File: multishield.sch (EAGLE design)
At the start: 15 parts, among them J1 3p-2.54, J2 2x16p-2.54, J4 2x6p-2.54, K2 TS-1101F, M1 ARDUINO_R3_ICSP, Q1 BC547CZ1G, SW1 SK-12D01, U1 AD595AQ-DIP14, U2 ATMEGA328P_PDIP

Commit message: various improvements + clock
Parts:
- removed Q1: BC547CZ1G, Seeed-OPL-Transistor:DIP-TRANSISTOR-NPN-45V-0.1A-BC547CZ1G(TO-92)
- added C2, C3: 22pf, Seeed-OPL-Capacitor:DIP-CERAMIC-DISC-22PF-50V-10%-NPO(D4.0MM)
- added Q2: (no value), SparkFun-DiscreteSemi:TRANSISTOR_NPNBC547
- added Y1: 16MHZ, Seeed-OPL-Crystal-Oscillator:DIP-CRYSTAL-16MHZ-18PF-30PPM-50R(HC49US)
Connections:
- new net N$55: C2.2, U2.PB7(XTAL2/TOSC2), Y1.2
- new net N$57: C3.1, U2.PB6(XTAL1/TOSC1), Y1.1
- net GND: now also C2.1, C3.2, Q2.E; no longer Q1.E
- net N$36: now also Q2.C; no longer Q1.C
- net N$38: now also Q2.B; no longer Q1.B
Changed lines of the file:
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@@
 <part name="K2" library="Seeed-OPL-Button" deviceset="DIP-BUTTON-FRONT-WHITE(2P-3.4X6MM)" device="" value="TS-1101F"/>
 <part name="C1" library="Seeed-OPL-Capacitor" deviceset="DIP-CAP-ALUMINUM-47UF-16V(D5-H9MM)" device="" value="100µF/16V  5X7"/>
-<part name="Q1" library="Seeed-OPL-Transistor" deviceset="DIP-TRANSISTOR-NPN-45V-0.1A-BC547CZ1G(TO-92)" device="" value="BC547CZ1G"/>
 <part name="GND5" library="supply1" deviceset="GND" device=""/>
 <part name="R1" library="Seeed-OPL-Resistor" deviceset="DIP-RES-1K-5%-1/4W(PR-D2.3XL6.5MM)" device="" value="1K"/>
@@
 <part name="GND6" library="supply1" deviceset="GND" device=""/>
 <part name="P+7" library="supply1" deviceset="VCC" device=""/>
+<part name="Y1" library="Seeed-OPL-Crystal-Oscillator" deviceset="DIP-CRYSTAL-16MHZ-18PF-30PPM-50R(HC49US)" device="" value="16MHZ"/>
+<part name="C2" library="Seeed-OPL-Capacitor" deviceset="DIP-CERAMIC-DISC-22PF-50V-10%-NPO(D4.0MM)" device="" value="22pf"/>
+<part name="C3" library="Seeed-OPL-Capacitor" deviceset="DIP-CERAMIC-DISC-22PF-50V-10%-NPO(D4.0MM)" device="" value="22pf"/>
+<part name="GND9" library="supply1" deviceset="GND" device=""/>
+<part name="Q2" library="SparkFun-DiscreteSemi" deviceset="TRANSISTOR_NPN" device="BC547"/>
 </parts>
 <sheets>
@@
 <instance part="K2" gate="G$1" x="318.77" y="45.72"/>
 <instance part="C1" gate="G$1" x="187.96" y="172.72"/>
-<instance part="Q1" gate="G$1" x="194.31" y="177.8" rot="R180"/>
 <instance part="GND5" gate="1" x="191.77" y="185.42" rot="R180"/>
 <instance part="R1" gate="G$1" x="208.28" y="177.8"/>
@@
 <instance part="GND6" gate="1" x="87.63" y="66.04" rot="R270"/>
 <instance part="P+7" gate="VCC" x="87.63" y="69.85" rot="R90"/>
+<instance part="Y1" gate="G$1" x="316.23" y="82.55" rot="R90"/>
+<instance part="C2" gate="G$1" x="321.31" y="91.44" rot="R180"/>
+<instance part="C3" gate="G$1" x="321.31" y="74.93"/>
+<instance part="GND9" gate="1" x="327.66" y="83.82" rot="R90"/>
+<instance part="Q2" gate="G$1" x="194.31" y="177.8" rot="R180"/>
 </instances>
 <busses>
@@
 </segment>
 <segment>
-<pinref part="Q1" gate="G$1" pin="E"/>
-<pinref part="GND5" gate="1" pin="GND"/>
-</segment>
-<segment>
 <pinref part="J1" gate="G$1" pin="P$3"/>
 <pinref part="GND6" gate="1" pin="GND"/>
+</segment>
+<segment>
+<pinref part="C3" gate="G$1" pin="2"/>
+<pinref part="C2" gate="G$1" pin="1"/>
+<wire x1="325.12" y1="74.93" x2="325.12" y2="83.82" width="0.1524" layer="91"/>
+<junction x="325.12" y="83.82"/>
+<wire x1="325.12" y1="83.82" x2="325.12" y2="91.44" width="0.1524" layer="91"/>
+<pinref part="GND9" gate="1" pin="GND"/>
+</segment>
+<segment>
+<pinref part="GND5" gate="1" pin="GND"/>
+<pinref part="Q2" gate="G$1" pin="E"/>
 </segment>
 </net>
@@
 </segment>
 </net>
-<net name="N$36" class="0">
-<segment>
-<pinref part="C1" gate="G$1" pin="-"/>
-<pinref part="Q1" gate="G$1" pin="C"/>
-</segment>
-</net>
 <net name="N$37" class="0">
 <segment>
@@
 <net name="N$38" class="0">
 <segment>
-<pinref part="Q1" gate="G$1" pin="B"/>
 <wire x1="204.47" y1="177.8" x2="196.85" y2="177.8" width="0.1524" layer="91"/>
 <pinref part="R1" gate="G$1" pin="1"/>
+<pinref part="Q2" gate="G$1" pin="B"/>
 </segment>
 </net>
@@
 </segment>
 </net>
+<net name="N$55" class="0">
+<segment>
+<pinref part="U2" gate="G$1" pin="PB7(XTAL2/TOSC2)"/>
+<wire x1="304.8" y1="85.09" x2="307.34" y2="85.09" width="0.1524" layer="91"/>
+<wire x1="307.34" y1="85.09" x2="307.34" y2="88.9" width="0.1524" layer="91"/>
+<wire x1="307.34" y1="88.9" x2="316.23" y2="88.9" width="0.1524" layer="91"/>
+<pinref part="Y1" gate="G$1" pin="2"/>
+<wire x1="316.23" y1="88.9" x2="316.23" y2="86.36" width="0.1524" layer="91"/>
+<junction x="316.23" y="88.9"/>
+<wire x1="316.23" y1="88.9" x2="316.23" y2="91.44" width="0.1524" layer="91"/>
+<pinref part="C2" gate="G$1" pin="2"/>
+<wire x1="316.23" y1="91.44" x2="317.5" y2="91.44" width="0.1524" layer="91"/>
+</segment>
+</net>
+<net name="N$57" class="0">
+<segment>
+<pinref part="U2" gate="G$1" pin="PB6(XTAL1/TOSC1)"/>
+<wire x1="304.8" y1="80.01" x2="307.34" y2="80.01" width="0.1524" layer="91"/>
+<wire x1="307.34" y1="80.01" x2="307.34" y2="77.47" width="0.1524" layer="91"/>
+<wire x1="307.34" y1="77.47" x2="316.23" y2="77.47" width="0.1524" layer="91"/>
+<pinref part="Y1" gate="G$1" pin="1"/>
+<wire x1="316.23" y1="77.47" x2="316.23" y2="78.74" width="0.1524" layer="91"/>
+<junction x="316.23" y="77.47"/>
+<wire x1="316.23" y1="77.47" x2="316.23" y2="74.93" width="0.1524" layer="91"/>
+<pinref part="C3" gate="G$1" pin="1"/>
+<wire x1="316.23" y1="74.93" x2="317.5" y2="74.93" width="0.1524" layer="91"/>
+</segment>
+</net>
+<net name="N$36" class="0">
+<segment>
+<pinref part="C1" gate="G$1" pin="-"/>
+<pinref part="Q2" gate="G$1" pin="C"/>
+</segment>
+</net>

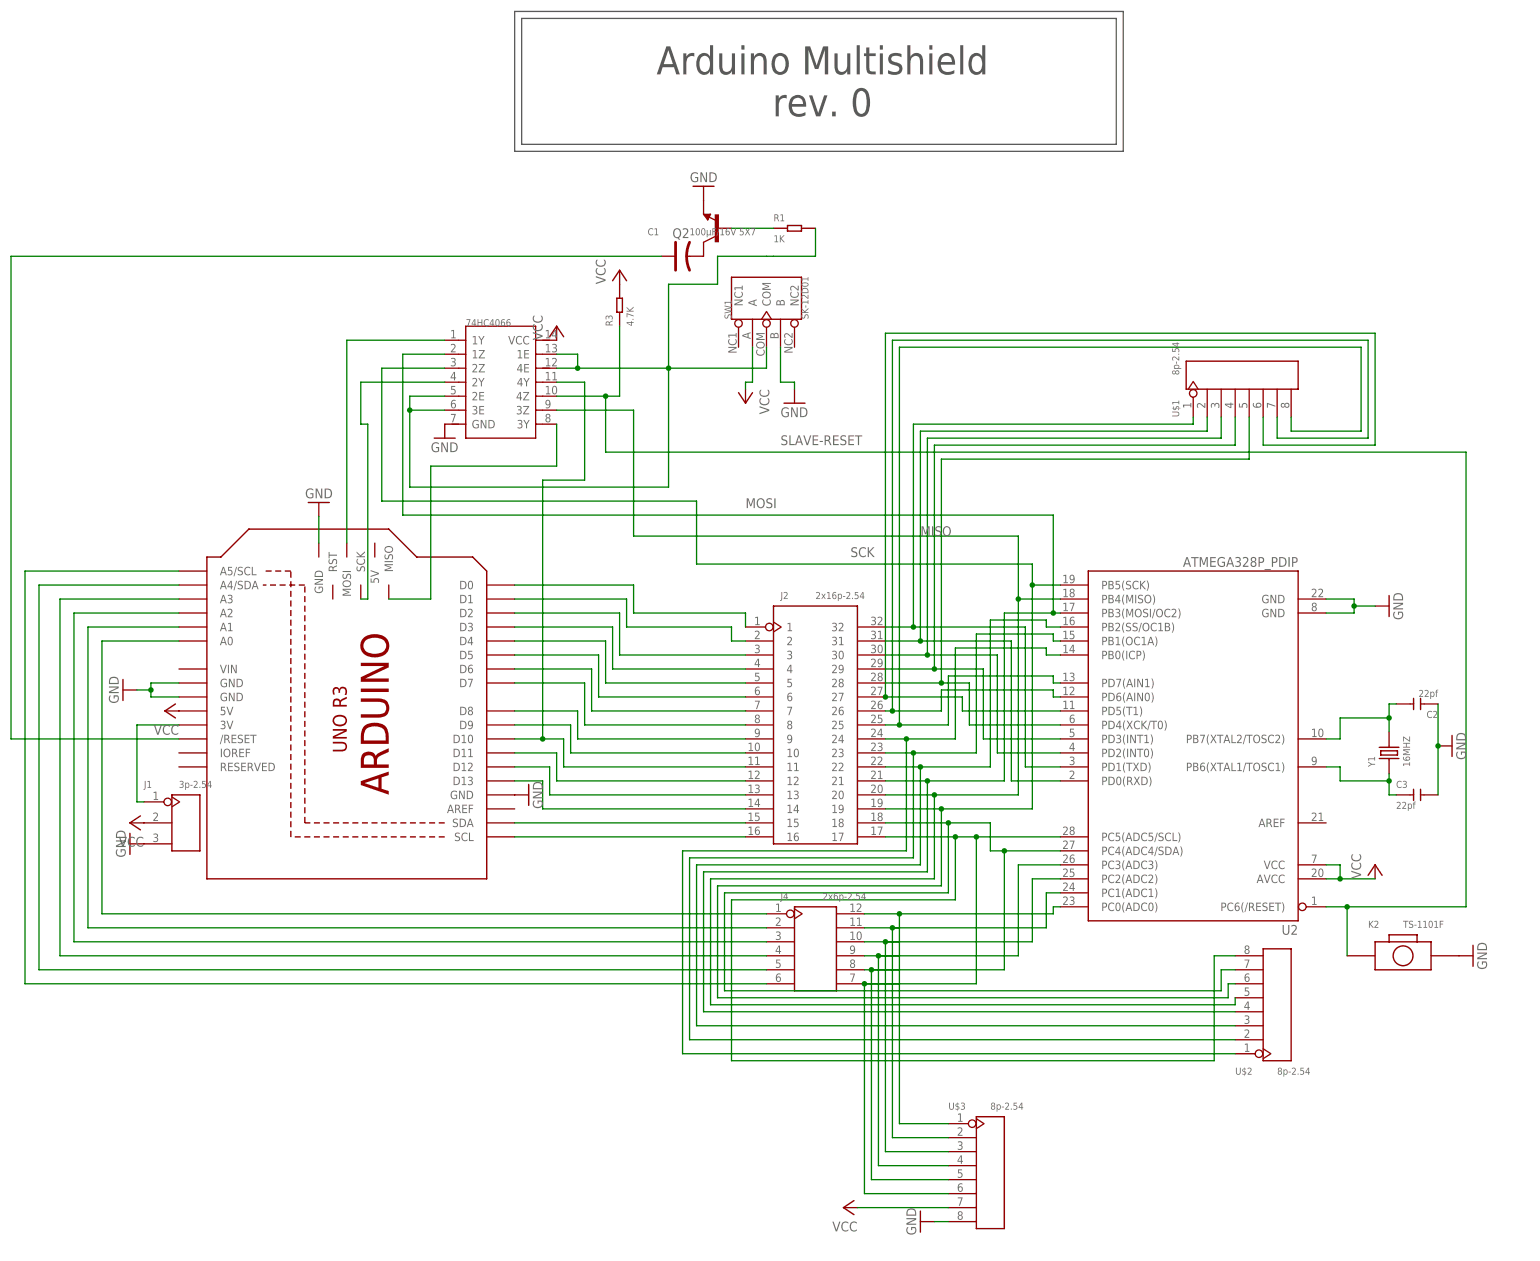
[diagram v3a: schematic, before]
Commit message: part replacements and bom
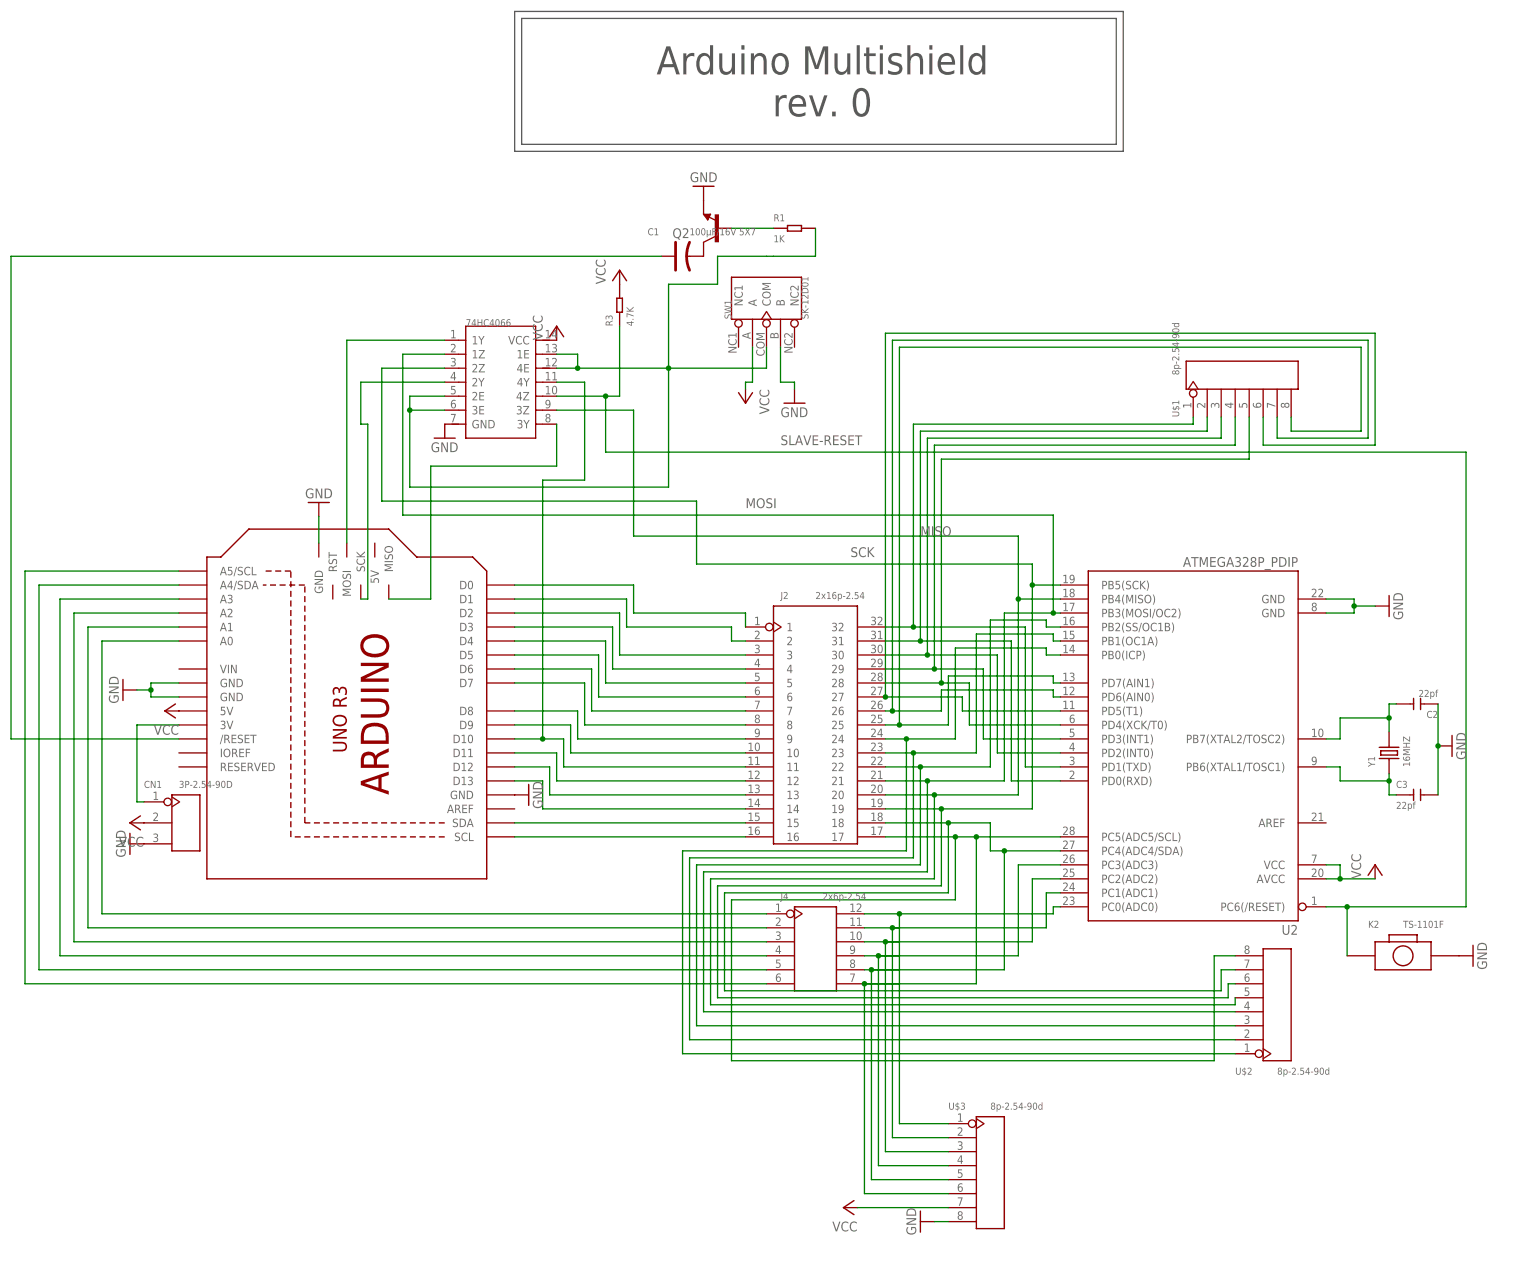
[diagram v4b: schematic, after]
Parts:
- removed J1: 3p-2.54, Seeed-OPL-Connector:DIP-BLACK-FEMALE-HEADER-VERT(3P-2.54)
- added CN1: 3P-2.54-90D, Seeed-OPL-Connector:DIP-BLACK-FEMALE-HEADER(3P-2.54-90D)
- U$1, U$2, U$3: value 8p-2.54 -> 8p-2.54-90d; device Seeed-OPL-Connector:DIP-BLACK-MALE-HEADER-VERT(8P-2.54) -> Seeed-OPL-Connector:DIP-BLACK-FEMALE-HEADER-R/A(8P-2.54-90D)
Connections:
- net GND: now also CN1.P$3; no longer J1.P$3
- net N$54: now also CN1.P$1; no longer J1.P$1
- net VCC: now also CN1.P$2; no longer J1.P$2
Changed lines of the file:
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@@
 <part name="R3" library="Seeed-OPL-Resistor" deviceset="DIP-RES-4.7K-5%-1/4W(PR-D2.3XL6.5MM)" device="" value="4.7K"/>
 <part name="P+5" library="supply1" deviceset="VCC" device=""/>
-<part name="U$1" library="Seeed-OPL-Connector" deviceset="DIP-BLACK-MALE-HEADER-VERT(8P-2.54)" device="" value="8p-2.54"/>
-<part name="U$2" library="Seeed-OPL-Connector" deviceset="DIP-BLACK-MALE-HEADER-VERT(8P-2.54)" device="" value="8p-2.54"/>
+<part name="U$1" library="Seeed-OPL-Connector" deviceset="DIP-BLACK-FEMALE-HEADER-R/A(8P-2.54-90D)" device="" value="8p-2.54-90d"/>
+<part name="U$2" library="Seeed-OPL-Connector" deviceset="DIP-BLACK-FEMALE-HEADER-R/A(8P-2.54-90D)" device="" value="8p-2.54-90d"/>
 <part name="GND8" library="supply1" deviceset="GND" device=""/>
-<part name="U$3" library="Seeed-OPL-Connector" deviceset="DIP-BLACK-MALE-HEADER-VERT(8P-2.54)" device="" value="8p-2.54"/>
+<part name="U$3" library="Seeed-OPL-Connector" deviceset="DIP-BLACK-FEMALE-HEADER-R/A(8P-2.54-90D)" device="" value="8p-2.54-90d"/>
 <part name="GND10" library="supply1" deviceset="GND" device=""/>
 <part name="P+6" library="supply1" deviceset="VCC" device=""/>
@@
 <part name="GND5" library="supply1" deviceset="GND" device=""/>
 <part name="R1" library="Seeed-OPL-Resistor" deviceset="DIP-RES-1K-5%-1/4W(PR-D2.3XL6.5MM)" device="" value="1K"/>
-<part name="J1" library="Seeed-OPL-Connector" deviceset="DIP-BLACK-FEMALE-HEADER-VERT(3P-2.54)" device="" value="3p-2.54"/>
 <part name="GND6" library="supply1" deviceset="GND" device=""/>
 <part name="P+7" library="supply1" deviceset="VCC" device=""/>
@@
 <part name="GND9" library="supply1" deviceset="GND" device=""/>
 <part name="Q2" library="SparkFun-DiscreteSemi" deviceset="TRANSISTOR_NPN" device="BC547"/>
+<part name="CN1" library="Seeed-OPL-Connector" deviceset="DIP-BLACK-FEMALE-HEADER(3P-2.54-90D)" device="" value="3P-2.54-90D"/>
 </parts>
 <sheets>
@@
 <instance part="GND5" gate="1" x="191.77" y="185.42" rot="R180"/>
 <instance part="R1" gate="G$1" x="208.28" y="177.8"/>
-<instance part="J1" gate="G$1" x="97.79" y="69.85"/>
 <instance part="GND6" gate="1" x="87.63" y="66.04" rot="R270"/>
 <instance part="P+7" gate="VCC" x="87.63" y="69.85" rot="R90"/>
@@
 <instance part="GND9" gate="1" x="327.66" y="83.82" rot="R90"/>
 <instance part="Q2" gate="G$1" x="194.31" y="177.8" rot="R180"/>
+<instance part="CN1" gate="G$1" x="97.79" y="69.85"/>
 </instances>
 <busses>
@@
 </segment>
 <segment>
-<pinref part="J1" gate="G$1" pin="P$2"/>
 <pinref part="P+7" gate="VCC" pin="VCC"/>
+<pinref part="CN1" gate="G$1" pin="P$2"/>
 </segment>
 </net>
@@
 </segment>
 <segment>
-<pinref part="J1" gate="G$1" pin="P$3"/>
-<pinref part="GND6" gate="1" pin="GND"/>
-</segment>
-<segment>
 <pinref part="C3" gate="G$1" pin="2"/>
 <pinref part="C2" gate="G$1" pin="1"/>
@@
 <pinref part="GND5" gate="1" pin="GND"/>
 <pinref part="Q2" gate="G$1" pin="E"/>
+</segment>
+<segment>
+<pinref part="GND6" gate="1" pin="GND"/>
+<pinref part="CN1" gate="G$1" pin="P$3"/>
 </segment>
 </net>
@@
 <net name="N$54" class="0">
 <segment>
-<pinref part="J1" gate="G$1" pin="P$1"/>
 <wire x1="90.17" y1="73.66" x2="88.9" y2="73.66" width="0.1524" layer="91"/>
 <wire x1="88.9" y1="73.66" x2="88.9" y2="87.63" width="0.1524" layer="91"/>
 <pinref part="M1" gate="G$1" pin="3V"/>
 <wire x1="88.9" y1="87.63" x2="96.52" y2="87.63" width="0.1524" layer="91"/>
-</segment>
-</net>
+<pinref part="CN1" gate="G$1" pin="P$1"/>
+</segment>
+</net>
